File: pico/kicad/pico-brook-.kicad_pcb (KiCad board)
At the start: 2 copper layers, 96.2 x 45.2 mm, 16 parts, among them J10 Conn_01x03_Male, J11 Conn_01x04_Female, J2 Conn_01x05_Male, J3 Screw_Terminal_01x20, J4 Conn_01x04_Male, J5 Conn_01x05_Male, J6 Conn_01x04_Male, J7 Conn_01x04_Male, J8 Conn_01x04_Male, J9 Conn_02x10_Odd_Even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

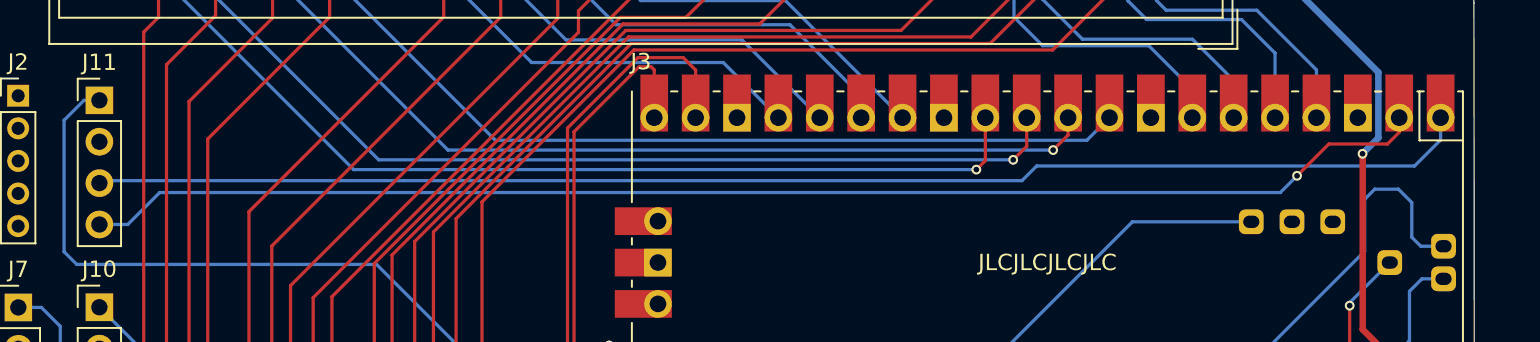
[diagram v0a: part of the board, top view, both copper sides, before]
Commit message: Swap OLED SDA and OLED SCL pins and headers on PCB and Schematic
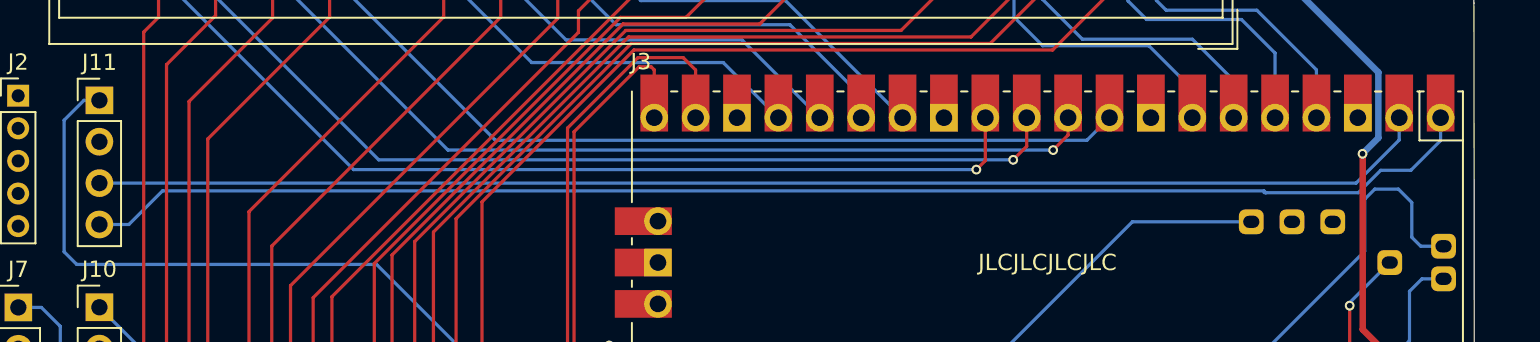
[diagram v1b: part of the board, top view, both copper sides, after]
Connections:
- U1 pad 1: OLED SCL -> OLED SDA
- U1 pad 2: OLED SDA -> OLED SCL
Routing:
- net OLED SDA: track 83.0 -> 86.0 mm, vias 1 -> 0
- net OLED SCL: track 84.8 -> 82.4 mm
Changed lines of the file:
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@@
     (fp_line (start -10.5 25.5) (end -10.5 -25.5) (layer "F.Fab") (width 0.12))
     (pad "1" smd rect locked (at -8.89 -24.13 270) (size 3.5 1.7) (drill (offset -0.9 0)) (layers "F.Cu" "F.Mask")
-      (net 6 "OLED SCL") (pinfunction "GPIO0") (pintype "bidirectional"))
+      (net 11 "OLED SDA") (pinfunction "GPIO0") (pintype "bidirectional"))
     (pad "1" thru_hole oval locked (at -8.89 -24.13 270) (size 1.7 1.7) (drill 1.02) (layers *.Cu *.Mask)
-      (net 6 "OLED SCL") (pinfunction "GPIO0") (pintype "bidirectional"))
+      (net 11 "OLED SDA") (pinfunction "GPIO0") (pintype "bidirectional"))
     (pad "2" smd rect locked (at -8.89 -21.59 270) (size 3.5 1.7) (drill (offset -0.9 0)) (layers "F.Cu" "F.Mask")
-      (net 11 "OLED SDA") (pinfunction "GPIO1") (pintype "bidirectional"))
+      (net 6 "OLED SCL") (pinfunction "GPIO1") (pintype "bidirectional"))
     (pad "2" thru_hole oval locked (at -8.89 -21.59 270) (size 1.7 1.7) (drill 1.02) (layers *.Cu *.Mask)
-      (net 11 "OLED SDA") (pinfunction "GPIO1") (pintype "bidirectional"))
+      (net 6 "OLED SCL") (pinfunction "GPIO1") (pintype "bidirectional"))
     (pad "3" smd rect locked (at -8.89 -19.05 270) (size 3.5 1.7) (drill (offset -0.9 0)) (layers "F.Cu" "F.Mask")
       (net 1 "GND") (pinfunction "GND") (pintype "power_in"))
@@
   (segment (start 130.41 85.15) (end 108.93 85.15) (width 0.2) (layer "B.Cu") (net 5))
   (segment (start 154.003059 90.0495) (end 135.3095 90.0495) (width 0.2) (layer "B.Cu") (net 5))
-  (segment (start 189.95 68.51) (end 189.95 67.145) (width 0.2) (layer "B.Cu") (net 6))
-  (segment (start 188.35 70.11) (end 189.95 68.51) (width 0.2) (layer "B.Cu") (net 6))
-  (segment (start 165.16 70.11) (end 188.35 70.11) (width 0.2) (layer "B.Cu") (net 6))
-  (segment (start 164.26 71.01) (end 165.16 70.11) (width 0.2) (layer "B.Cu") (net 6))
+  (segment (start 187.41 68.515) (end 184.765 71.16) (width 0.2) (layer "B.Cu") (net 6))
   (segment (start 107.64 71.16) (end 107.79 71.01) (width 0.2) (layer "B.Cu") (net 6))
-  (segment (start 107.79 71.01) (end 164.26 71.01) (width 0.2) (layer "B.Cu") (net 6))
+  (segment (start 184.765 71.16) (end 107.64 71.16) (width 0.2) (layer "B.Cu") (net 6))
+  (segment (start 187.41 67.145) (end 187.41 68.515) (width 0.2) (layer "B.Cu") (net 6))
   (segment (start 163.77 59.55) (end 161.13 62.19) (width 0.2) (layer "F.Cu") (net 7))
   (segment (start 128.14 74.162744) (end 128.14 95.41) (width 0.2) (layer "F.Cu") (net 7))
@@
   (segment (start 182.33 64.21) (end 182.33 67.145) (width 0.2) (layer "B.Cu") (net 10))
   (segment (start 169.38 56.25) (end 171.44 56.25) (width 0.2) (layer "B.Cu") (net 10))
-  (segment (start 186.69 68.76) (end 187.41 68.04) (width 0.2) (layer "F.Cu") (net 11))
-  (segment (start 183.09 68.76) (end 186.69 68.76) (width 0.2) (layer "F.Cu") (net 11))
-  (segment (start 181.1405 70.7095) (end 183.09 68.76) (width 0.2) (layer "F.Cu") (net 11))
-  (segment (start 187.41 68.04) (end 187.41 67.145) (width 0.2) (layer "F.Cu") (net 11))
-  (segment (start 181.14 70.7095) (end 181.1405 70.7095) (width 0.2) (layer "F.Cu") (net 11))
-  (via (at 181.14 70.7095) (size 0.6) (drill 0.35) (layers "F.Cu" "B.Cu") (net 11))
-  (segment (start 111.34 71.74) (end 109.38 73.7) (width 0.2) (layer "B.Cu") (net 11))
-  (segment (start 109.38 73.7) (end 107.64 73.7) (width 0.2) (layer "B.Cu") (net 11))
-  (segment (start 180.1095 71.74) (end 111.34 71.74) (width 0.2) (layer "B.Cu") (net 11))
-  (segment (start 181.14 70.7095) (end 180.1095 71.74) (width 0.2) (layer "B.Cu") (net 11))
+  (segment (start 179.125 71.75) (end 179.225 71.75) (width 0.2) (layer "B.Cu") (net 11))
+  (segment (start 189.95 68.55) (end 189.95 67.145) (width 0.2) (layer "B.Cu") (net 11))
+  (segment (start 186.275 70.375) (end 188.125 70.375) (width 0.2) (layer "B.Cu") (net 11))
+  (segment (start 179.111346 71.636346) (end 111.513654 71.636346) (width 0.2) (layer "B.Cu") (net 11))
+  (segment (start 188.125 70.375) (end 189.95 68.55) (width 0.2) (layer "B.Cu") (net 11))
+  (segment (start 179.225 71.75) (end 179.111346 71.636346) (width 0.2) (layer "B.Cu") (net 11))
+  (segment (start 109.45 73.7) (end 107.64 73.7) (width 0.2) (layer "B.Cu") (net 11))
+  (segment (start 179.225 71.75) (end 184.9 71.75) (width 0.2) (layer "B.Cu") (net 11))
+  (segment (start 184.9 71.75) (end 186.275 70.375) (width 0.2) (layer "B.Cu") (net 11))
+  (segment (start 111.513654 71.636346) (end 109.45 73.7) (width 0.2) (layer "B.Cu") (net 11))
   (segment (start 121.77 60.97) (end 114.29 68.45) (width 0.2) (layer "F.Cu") (net 12))
   (segment (start 121.77 58.36) (end 121.77 60.97) (width 0.2) (layer "F.Cu") (net 12))
